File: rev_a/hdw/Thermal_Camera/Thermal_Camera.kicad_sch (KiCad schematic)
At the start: 0 parts

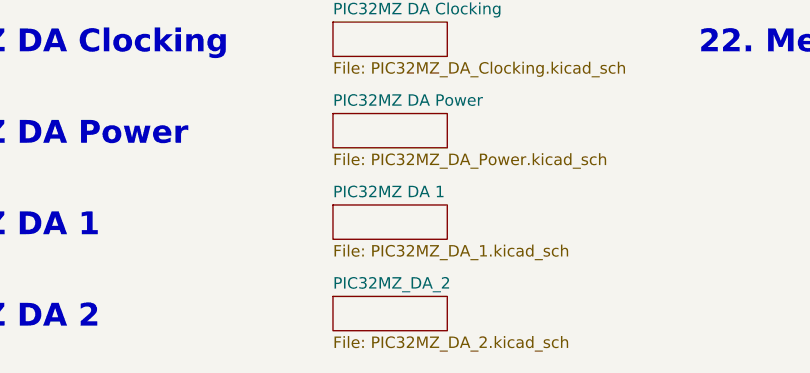
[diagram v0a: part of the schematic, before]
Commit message: copied lots of circuitry to reuse
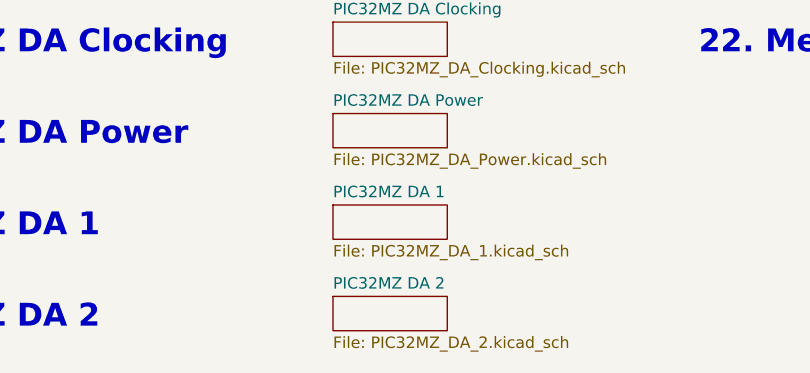
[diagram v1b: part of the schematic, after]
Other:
- sheet PIC32MZ_DA_2 renamed PIC32MZ DA 2
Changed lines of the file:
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@@
     (stroke (width 0.1524) (type solid))
     (fill (color 0 0 0 0.0000))
-    (property "Sheetname" "PIC32MZ_DA_2" (at 82.55 154.2284 0)
+    (property "Sheetname" "PIC32MZ DA 2" (at 82.55 154.2284 0)
       (effects (font (size 1.27 1.27)) (justify left bottom))
     )

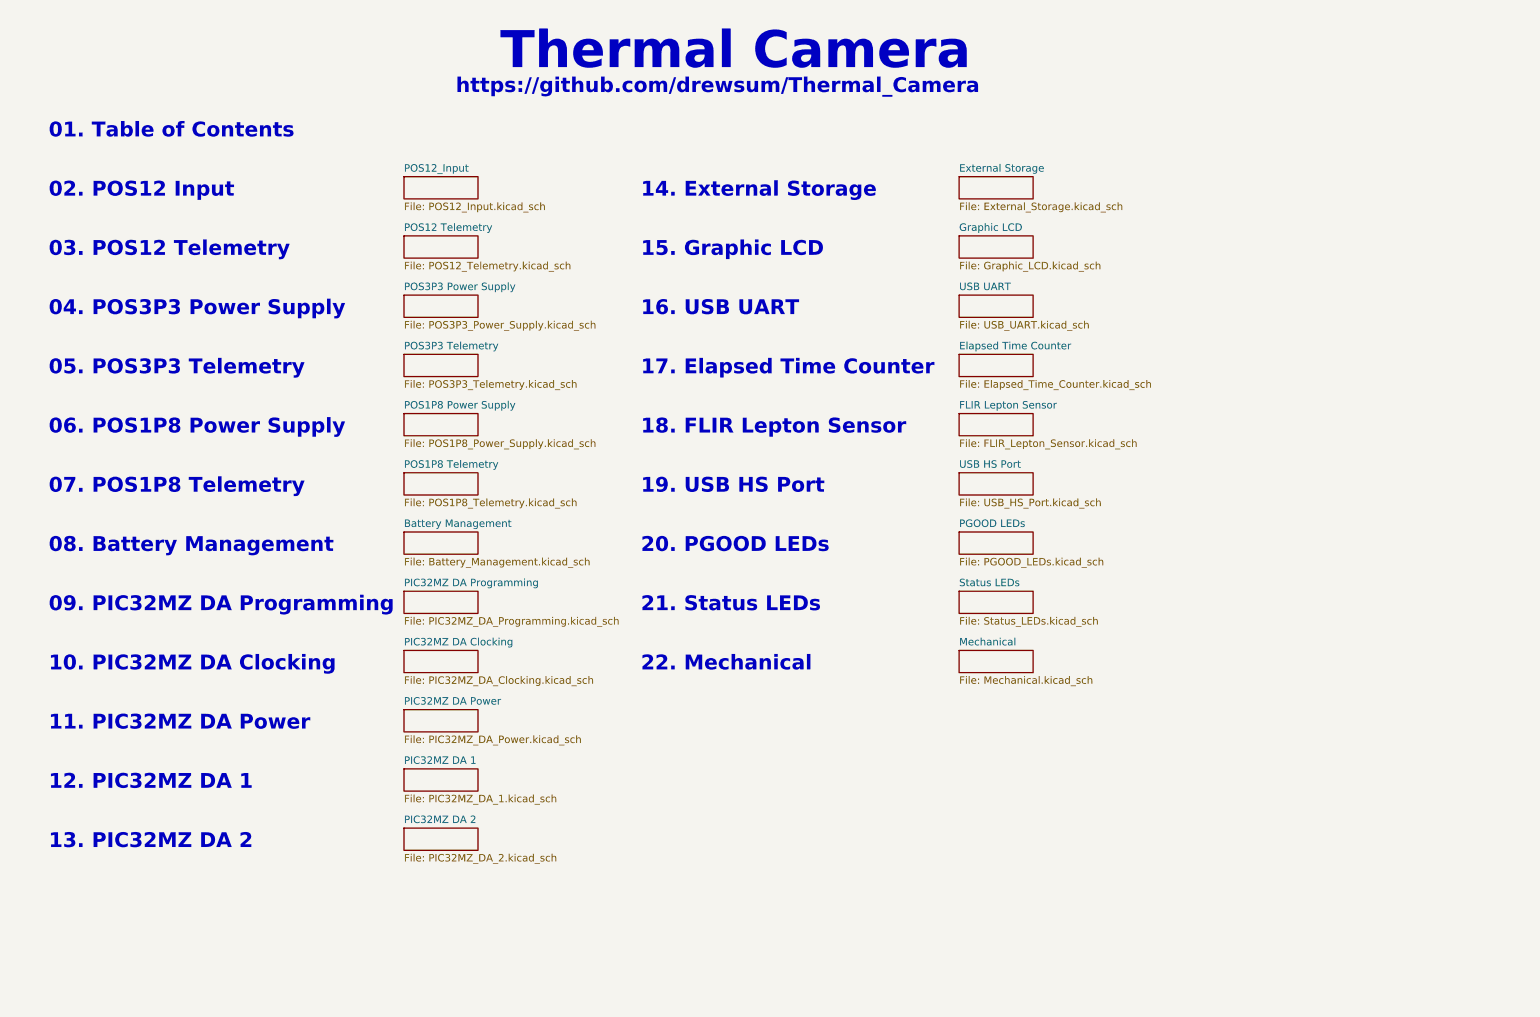
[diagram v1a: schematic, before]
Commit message: added lepton sensor, made some other schematic progress
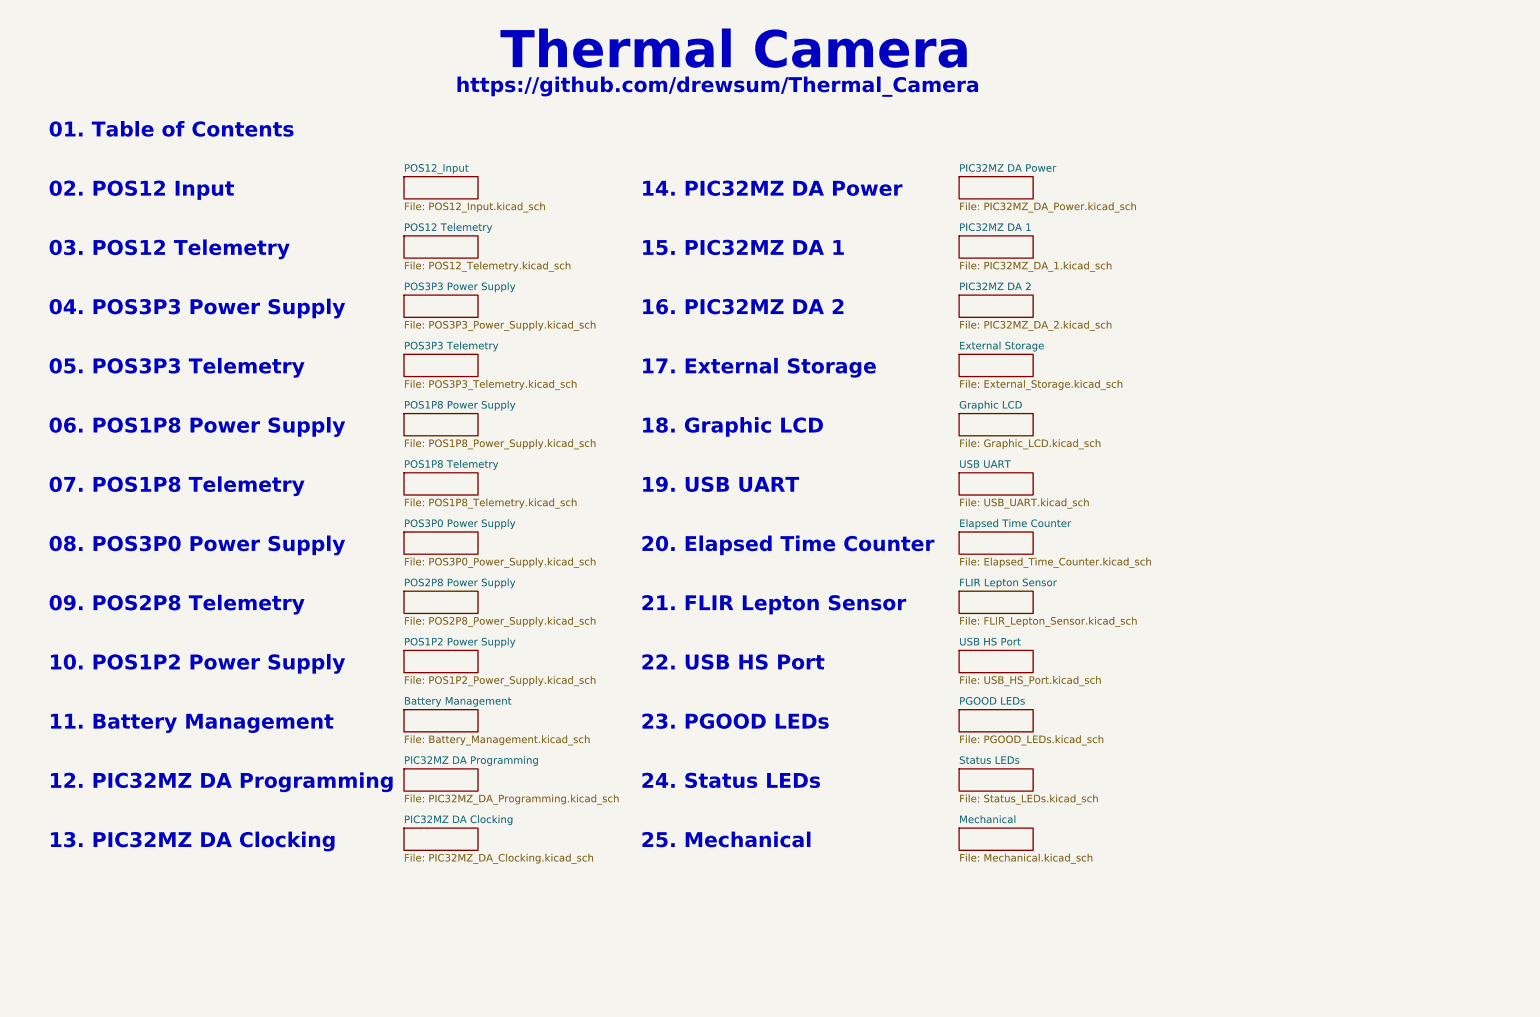
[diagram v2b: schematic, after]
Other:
- added sheet POS1P2 Power Supply (POS1P2_Power_Supply.kicad_sch)
- added sheet POS2P8 Power Supply (POS2P8_Power_Supply.kicad_sch)
- added sheet POS3P0 Power Supply (POS3P0_Power_Supply.kicad_sch)
- note added: "08. POS3P0 Power Supply"
- note added: "09. POS2P8 Telemetry"
- note added: "10. POS1P2 Power Supply"
- note added: "11. Battery Management"
- note added: "12. PIC32MZ DA Programming"
- note added: "13. PIC32MZ DA Clocking"
- note added: "14. PIC32MZ DA Power"
- note added: "15. PIC32MZ DA 1"
- note added: "16. PIC32MZ DA 2"
- note added: "17. External Storage"
- note added: "18. Graphic LCD"
- note added: "19. USB UART"
- note added: "20. Elapsed Time Counter"
- note added: "21. FLIR Lepton Sensor"
- note added: "22. USB HS Port"
- note added: "23. PGOOD LEDs"
- note added: "24. Status LEDs"
- note added: "25. Mechanical"
- note removed: "08. Battery Management"
- note removed: "09. PIC32MZ DA Programming"
- note removed: "10. PIC32MZ DA Clocking"
- note removed: "11. PIC32MZ DA Power"
- note removed: "12. PIC32MZ DA 1"
- note removed: "13. PIC32MZ DA 2"
- note removed: "14. External Storage"
- note removed: "15. Graphic LCD"
- note removed: "16. USB UART"
- note removed: "17. Elapsed Time Counter"
- note removed: "18. FLIR Lepton Sensor"
- note removed: "19. USB HS Port"
- note removed: "20. PGOOD LEDs"
- note removed: "21. Status LEDs"
- note removed: "22. Mechanical"

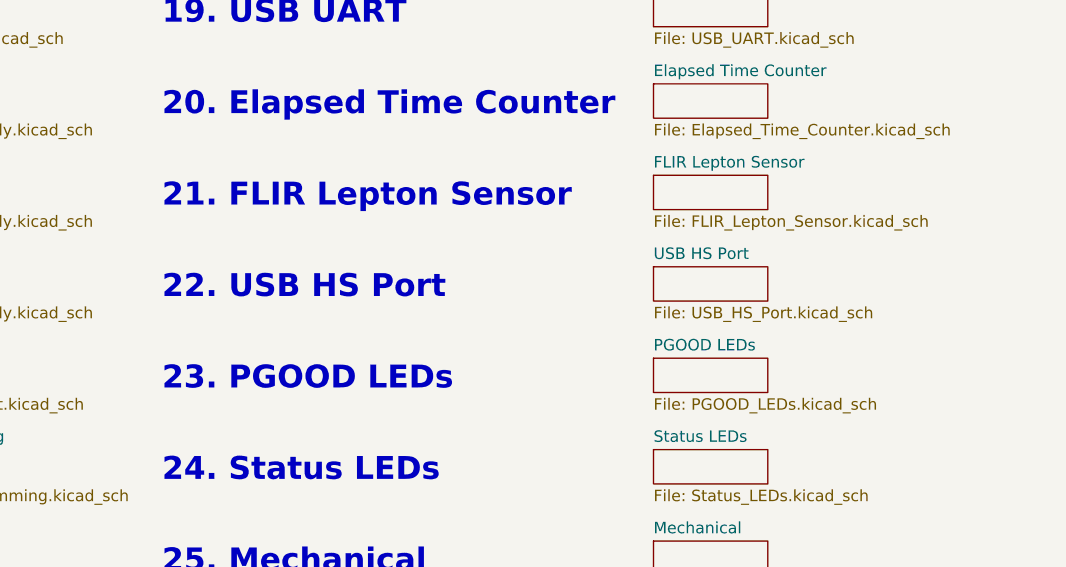
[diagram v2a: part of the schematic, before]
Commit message: changed USB HS port to hub
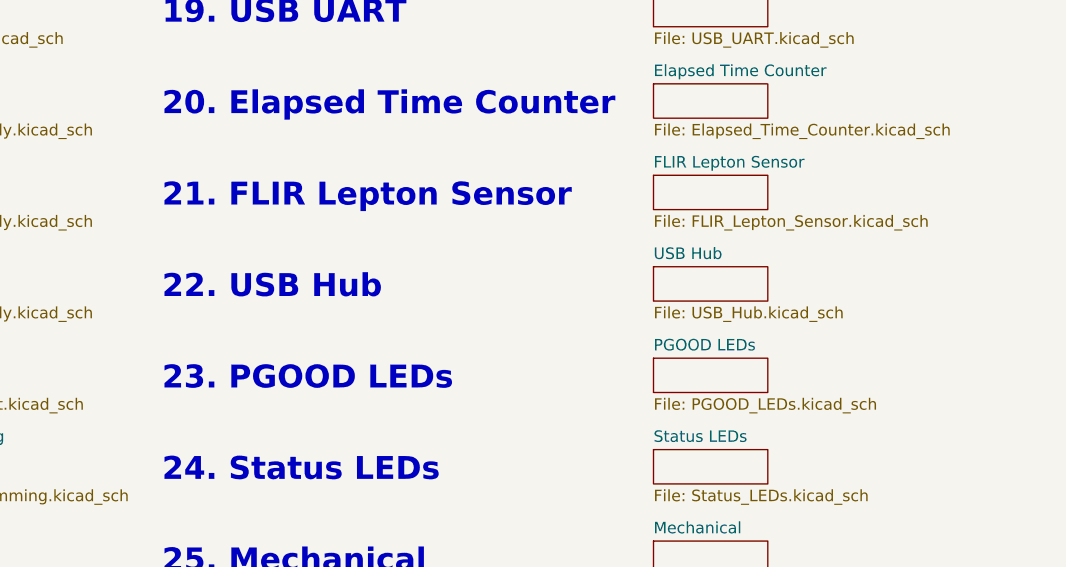
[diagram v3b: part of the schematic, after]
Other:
- sheet USB HS Port renamed USB Hub
- sheet USB Hub: file USB_HS_Port.kicad_sch -> USB_Hub.kicad_sch
- note added: "22. USB Hub"
- note removed: "22. USB HS Port"
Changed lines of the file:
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@@
     (effects (font (face "Courier New") (size 2.54 2.54) (thickness 0.508) bold) (justify left bottom))
   )
-  (text "22. USB HS Port" (at 123.19 128.27 0)
+  (text "22. USB Hub" (at 123.19 128.27 0)
     (effects (font (face "Courier New") (size 2.54 2.54) (thickness 0.508) bold) (justify left bottom))
   )
@@
     (stroke (width 0.1524) (type solid))
     (fill (color 0 0 0 0.0000))
-    (property "Sheetname" "USB HS Port" (at 177.8 123.7484 0)
+    (property "Sheetname" "USB Hub" (at 177.8 123.7484 0)
       (effects (font (size 1.27 1.27)) (justify left bottom))
     )
-    (property "Sheetfile" "USB_HS_Port.kicad_sch" (at 177.8 128.8546 0)
+    (property "Sheetfile" "USB_Hub.kicad_sch" (at 177.8 128.8546 0)
       (effects (font (size 1.27 1.27)) (justify left top))
     )

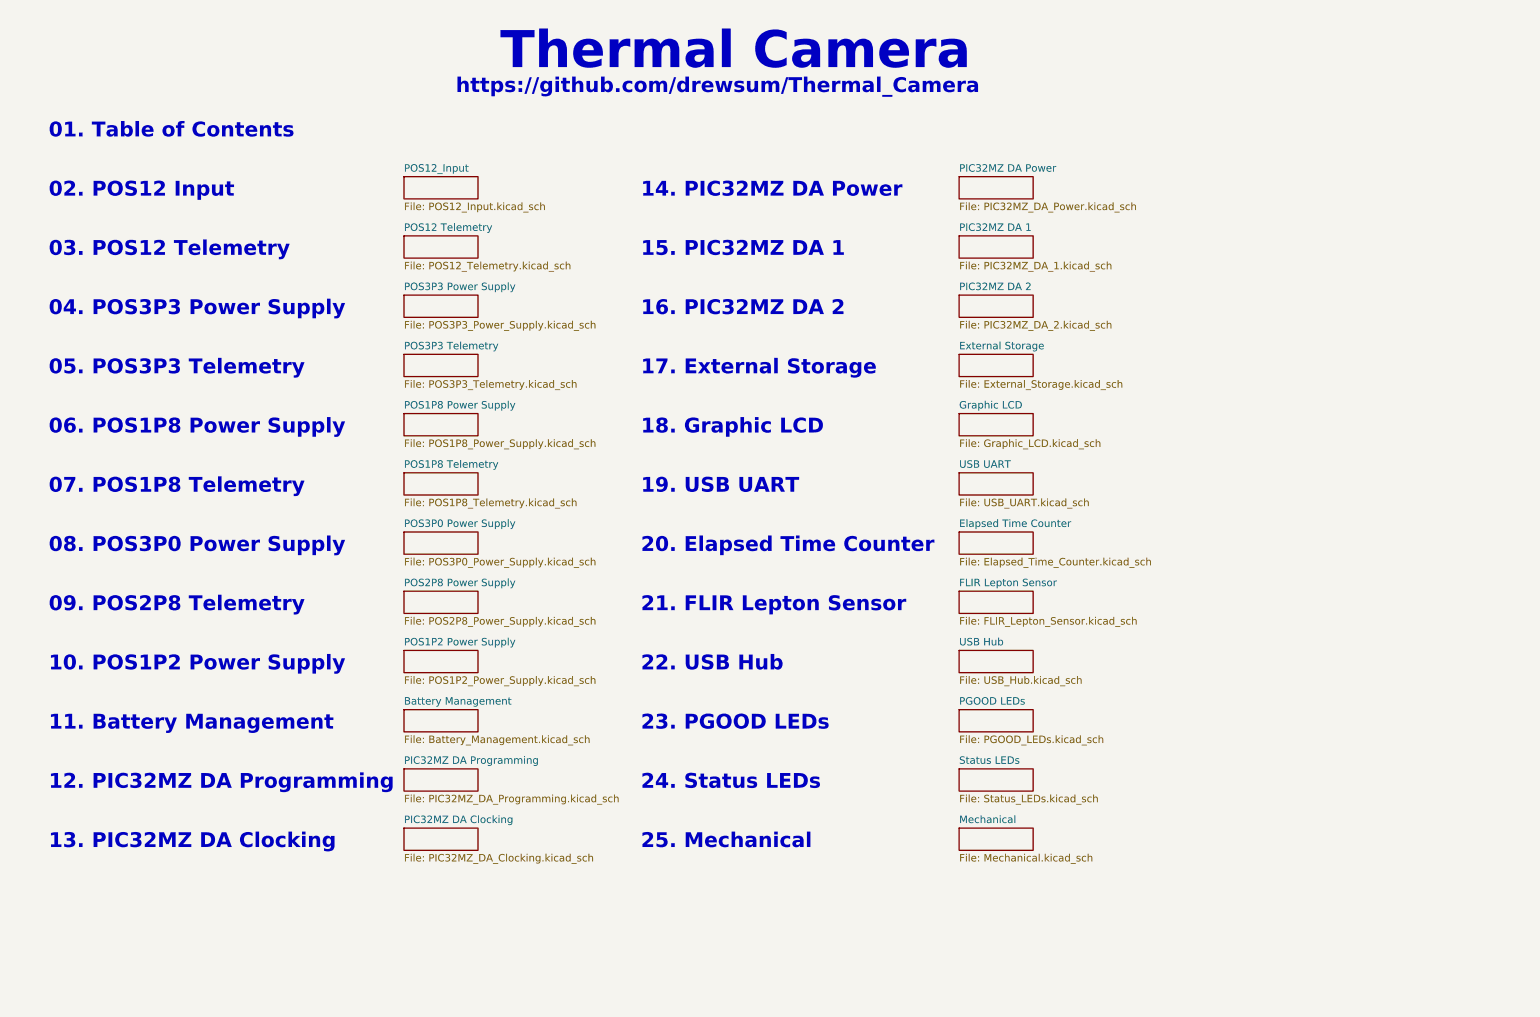
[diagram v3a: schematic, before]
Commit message: added many more blank schematic sheets
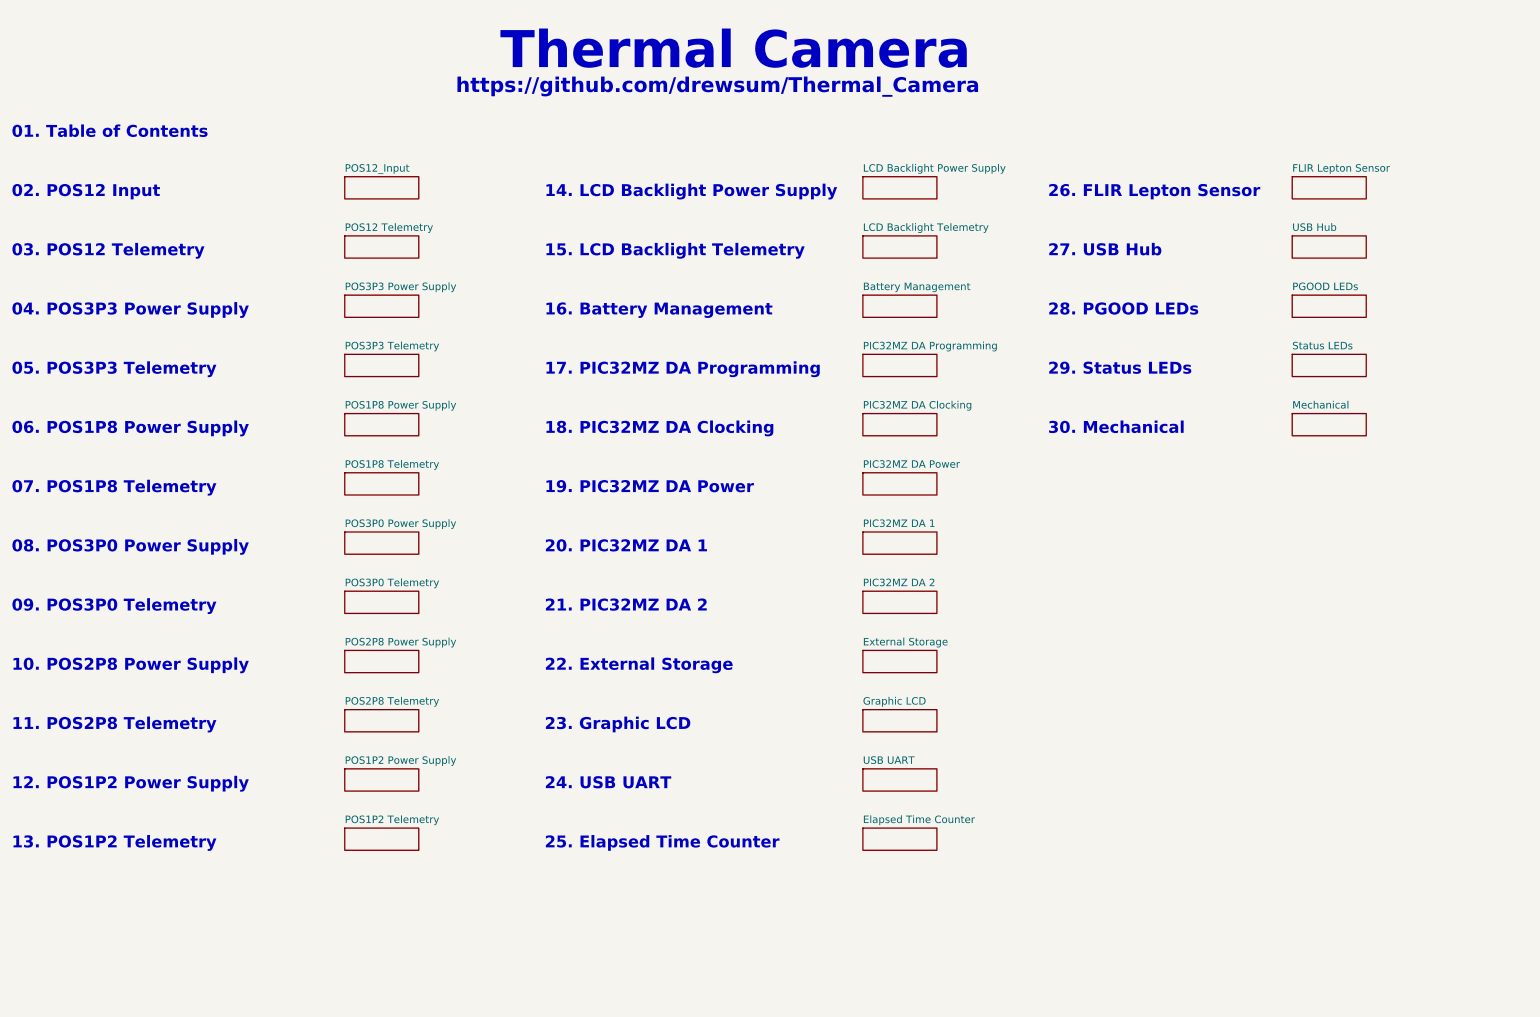
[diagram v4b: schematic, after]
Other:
- added sheet LCD Backlight Power Supply (LCD_Backlight_Power_Supply.kicad_sch)
- added sheet LCD Backlight Telemetry (LCD_Backlight_Telemetry.kicad_sch)
- added sheet POS1P2 Telemetry (POS1P2_Telemetry.kicad_sch)
- added sheet POS2P8 Telemetry (POS2P8_Telemetry.kicad_sch)
- added sheet POS3P0 Telemetry (POS3P0_Telemetry.kicad_sch)
- note added: "09. POS3P0 Telemetry"
- note added: "10. POS2P8 Power Supply"
- note added: "11. POS2P8 Telemetry"
- note added: "12. POS1P2 Power Supply"
- note added: "13. POS1P2 Telemetry"
- note added: "14. LCD Backlight Power Supply"
- note added: "15. LCD Backlight Telemetry"
- note added: "16. Battery Management"
- note added: "17. PIC32MZ DA Programming"
- note added: "18. PIC32MZ DA Clocking"
- note added: "19. PIC32MZ DA Power"
- note added: "20. PIC32MZ DA 1"
- note added: "21. PIC32MZ DA 2"
- note added: "22. External Storage"
- note added: "23. Graphic LCD"
- note added: "24. USB UART"
- note added: "25. Elapsed Time Counter"
- note added: "26. FLIR Lepton Sensor"
- note added: "27. USB Hub"
- note added: "28. PGOOD LEDs"
- note added: "29. Status LEDs"
- note added: "30. Mechanical"
- note removed: "09. POS2P8 Telemetry"
- note removed: "10. POS1P2 Power Supply"
- note removed: "11. Battery Management"
- note removed: "12. PIC32MZ DA Programming"
- note removed: "13. PIC32MZ DA Clocking"
- note removed: "14. PIC32MZ DA Power"
- note removed: "15. PIC32MZ DA 1"
- note removed: "16. PIC32MZ DA 2"
- note removed: "17. External Storage"
- note removed: "18. Graphic LCD"
- note removed: "19. USB UART"
- note removed: "20. Elapsed Time Counter"
- note removed: "21. FLIR Lepton Sensor"
- note removed: "22. USB Hub"
- note removed: "23. PGOOD LEDs"
- note removed: "24. Status LEDs"
- note removed: "25. Mechanical"
